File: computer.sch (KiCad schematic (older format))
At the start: 0 parts

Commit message: ram pcb
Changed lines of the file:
@@
 $Descr A4 11693 8268
 encoding utf-8
-Sheet 1 13
+Sheet 1 12
 Title ""
 Date ""
@@
 Wire Bus Line
 	5100 2025 4725 2025
-$Sheet
-S 3575 2750 1100 775
-U 5D35D52D
-F0 "RAM" 50
-F1 "RAM.sch" 50
-F2 "A_BUS[0..15]" I L 3575 2850 50
-F3 "D_BUS[0..15]" B R 4675 3075 50
-F4 "~WE~" I L 3575 3000 50
-F5 "~CE~" I L 3575 3100 50
-F6 "~OE~" I L 3575 3200 50
-F7 "P[0..15]" I L 3575 3450 50
-F8 "~ENABLE_OUTPUT~" I L 3575 3300 50
-$EndSheet
 Wire Bus Line
 	5075 3075 4675 3075
@@
 Wire Bus Line
 	3275 2850 3575 2850
+$Sheet
+S 3575 2775 1100 625
+U 5EEA4AC8
+F0 "RAM" 50
+F1 "memory/memory.sch" 50
+F2 "A[0..15]" I L 3575 2850 50
+F3 "D[0..15]" B R 4675 3075 50
+F4 "~BE~" I L 3575 2975 50
+F5 "~R~-W" I L 3575 3075 50
+$EndSheet
 $EndSCHEMATC

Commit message: program counter
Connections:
- wire segments 8 -> 10
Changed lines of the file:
@@
 	4700 1175 5000 1175
-Wire Wire Line
-	5000 1175 5000 1875
 Wire Wire Line
 	6250 1875 5000 1875
@@
 Wire Bus Line
 	5100 3075 6250 3075
-Wire Bus Line
-	5100 1175 5100 2025
 Connection ~ 5100 2025
 Wire Bus Line
@@
 F5 "~R~-W" I L 3575 3075 50
 $EndSheet
+$Sheet
+S 6250 975  850  550
+U 5EEFDD90
+F0 "program counter" 50
+F1 "program_counter/program_counter.sch" 50
+F2 "BUS[0..15]" B L 6250 1100 50
+F3 "CLK" I L 6250 1300 50
+F4 "~RESET~" I R 7100 1200 50
+F5 "~LOAD~" I R 7100 1300 50
+F6 "COUNT" I R 7100 1400 50
+F7 "~EO~" I R 7100 1100 50
+$EndSheet
+Wire Bus Line
+	6250 1100 5100 1100
+Wire Bus Line
+	5100 1100 5100 2025
+Wire Wire Line
+	6250 1300 5000 1300
+Wire Wire Line
+	5000 1175 5000 1300
+Connection ~ 5000 1300
+Wire Wire Line
+	5000 1300 5000 1875
 $EndSCHEMATC

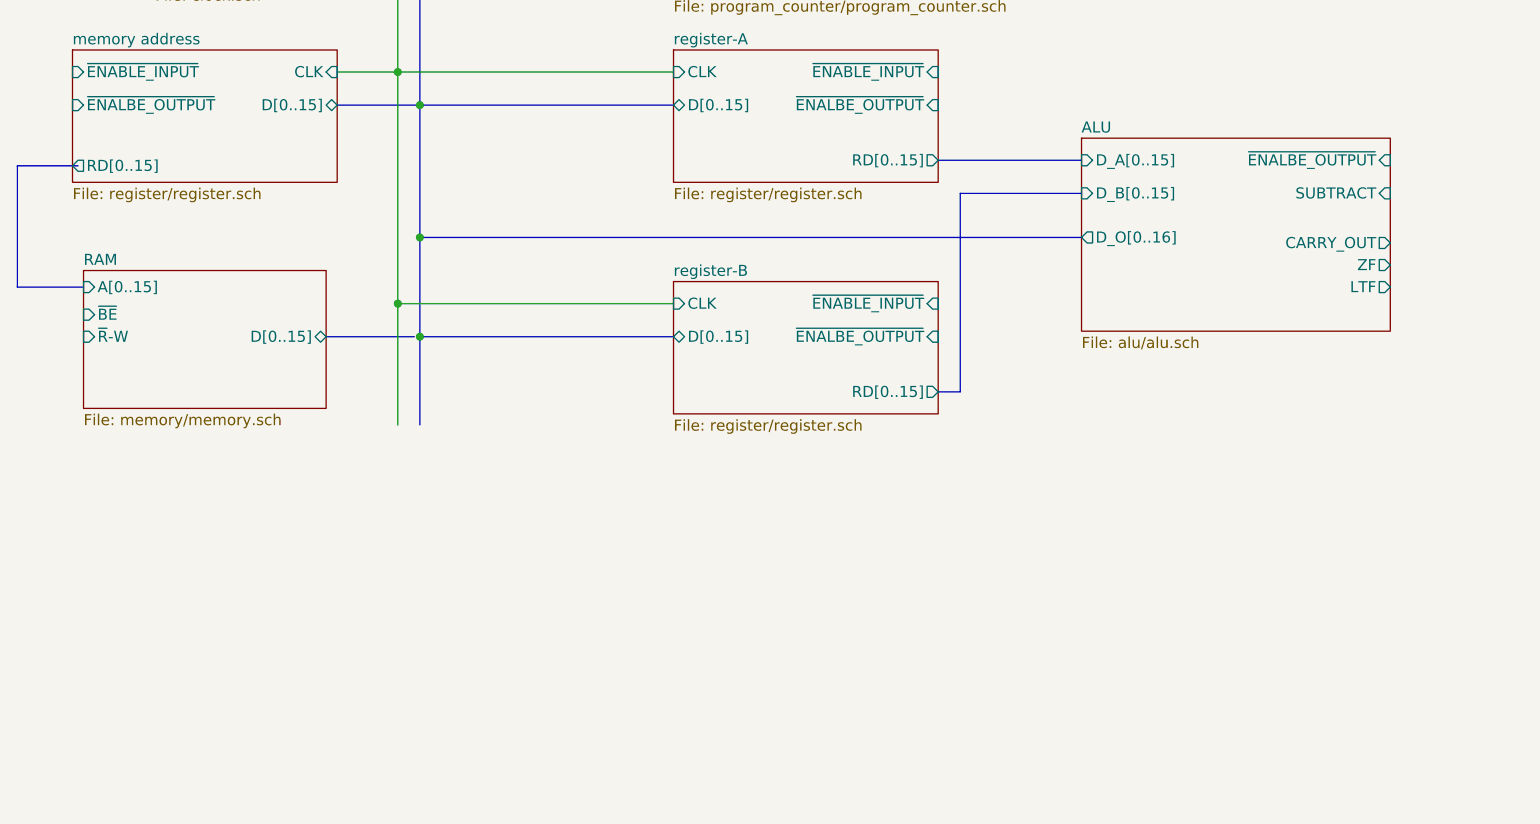
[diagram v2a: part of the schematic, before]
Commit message: add bit operations
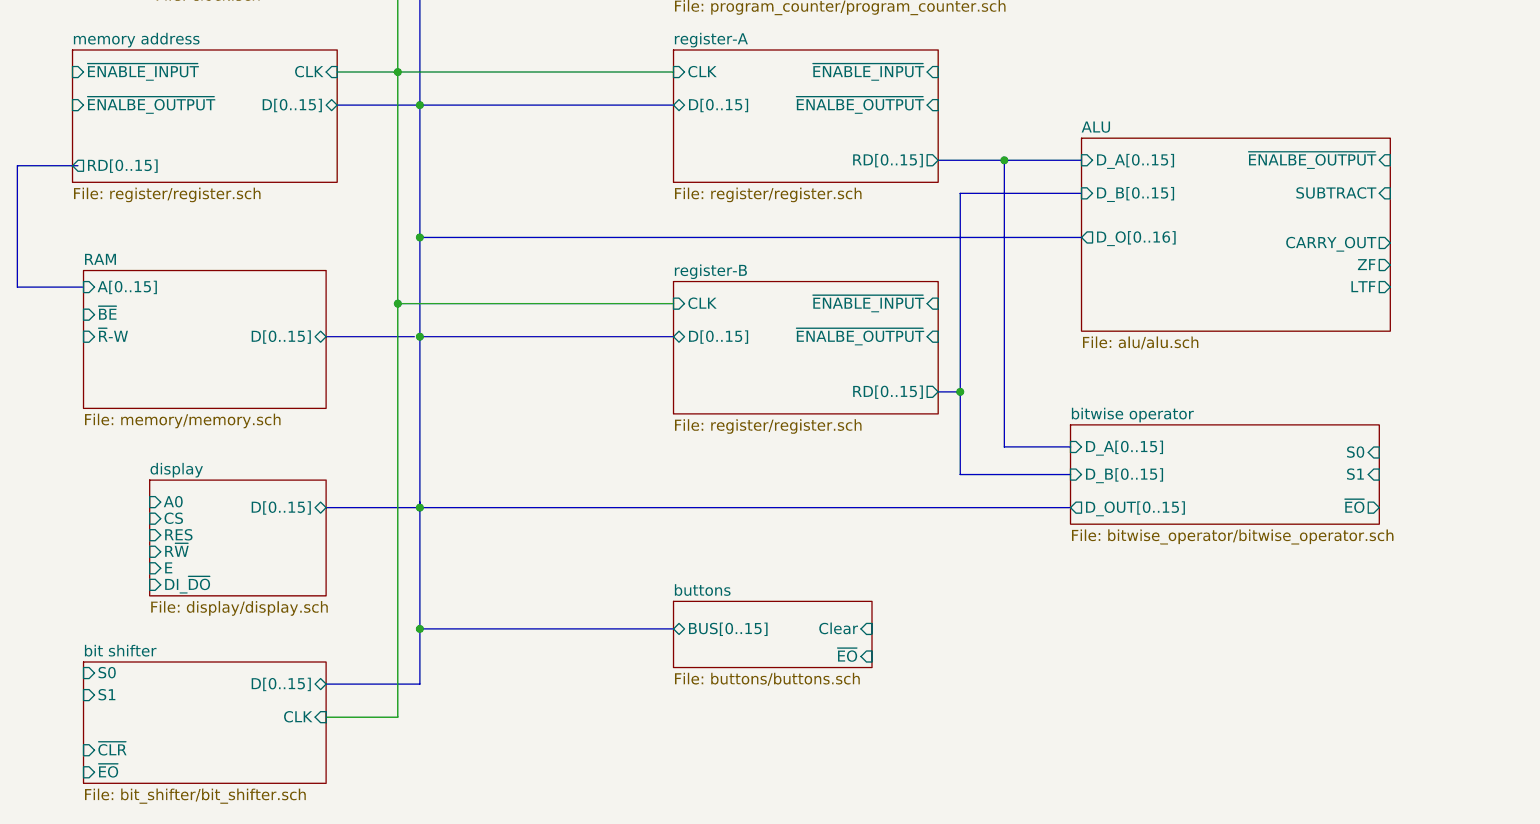
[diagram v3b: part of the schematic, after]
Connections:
- wire segments 10 -> 11
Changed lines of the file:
@@
 $Descr A4 11693 8268
 encoding utf-8
-Sheet 1 12
+Sheet 1 29
 Title ""
 Date ""
@@
 	6250 2925 5000 2925
 Connection ~ 5000 2925
-Wire Wire Line
-	5000 2925 5000 3475
 Wire Bus Line
 	6250 2025 5100 2025
@@
 	5100 2025 5100 2625
 Connection ~ 5100 3075
-Wire Bus Line
-	5100 3075 5100 3475
 $Sheet
 S 8100 2175 1400 875
@@
 $EndSheet
 Wire Bus Line
-	7450 2275 8100 2275
+	7450 2275 7750 2275
 Wire Bus Line
 	7450 3325 7550 3325
-Wire Bus Line
-	7550 3325 7550 2425
 Wire Bus Line
 	7550 2425 8100 2425
@@
 Wire Wire Line
 	5000 1300 5000 1875
+$Sheet
+S 8050 3475 1400 450
+U 5F3A84CD
+F0 "bitwise operator" 50
+F1 "bitwise_operator/bitwise_operator.sch" 50
+F2 "D_A[0..15]" I L 8050 3575 50
+F3 "D_B[0..15]" I L 8050 3700 50
+F4 "S0" I R 9450 3600 50
+F5 "S1" I R 9450 3700 50
+F6 "D_OUT[0..15]" O L 8050 3850 50
+F7 "~EO~" O R 9450 3850 50
+$EndSheet
+Wire Bus Line
+	8050 3700 7550 3700
+Wire Bus Line
+	7550 2425 7550 3325
+Connection ~ 7550 3325
+Wire Bus Line
+	7550 3325 7550 3700
+Wire Bus Line
+	8050 3575 7750 3575
+Wire Bus Line
+	7750 3575 7750 2275
+Connection ~ 7750 2275
+Wire Bus Line
+	7750 2275 8100 2275
+Wire Bus Line
+	8050 3850 5100 3850
+Wire Bus Line
+	5100 3075 5100 3850
+$Sheet
+S 6250 4275 900  300
+U 5F3A94D5
+F0 "buttons" 50
+F1 "buttons/buttons.sch" 50
+F2 "Clear" I R 7150 4400 50
+F3 "~EO~" I R 7150 4525 50
+F4 "BUS[0..15]" B L 6250 4400 50
+$EndSheet
+Wire Bus Line
+	5100 3850 5100 4400
+Wire Bus Line
+	5100 4400 6250 4400
+Connection ~ 5100 3850
+Wire Bus Line
+	5100 3850 5100 3825
+$Sheet
+S 3575 4550 1100 550
+U 5F3AB933
+F0 "bit shifter" 50
+F1 "bit_shifter/bit_shifter.sch" 50
+F2 "D[0..15]" B R 4675 4650 50
+F3 "S0" I L 3575 4600 50
+F4 "S1" I L 3575 4700 50
+F5 "CLK" I R 4675 4800 50
+F6 "~CLR~" I L 3575 4950 50
+F7 "~EO~" I L 3575 5050 50
+$EndSheet
+Wire Bus Line
+	5100 4400 5100 4650
+Wire Bus Line
+	5100 4650 4675 4650
+Connection ~ 5100 4400
+Wire Wire Line
+	5000 4800 4675 4800
+Wire Wire Line
+	5000 2925 5000 4800
+Wire Bus Line
+	4675 3850 5100 3850
+$Sheet
+S 3875 3725 800  525
+U 5F3B052B
+F0 "display" 50
+F1 "display/display.sch" 50
+F2 "D[0..15]" B R 4675 3850 50
+F3 "A0" I L 3875 3825 50
+F4 "CS" I L 3875 3900 50
+F5 "RES" I L 3875 3975 50
+F6 "R~W~" I L 3875 4050 50
+F7 "E" I L 3875 4125 50
+F8 "DI_~DO~" I L 3875 4200 50
+$EndSheet
 $EndSCHEMATC

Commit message: memory programmer and cu
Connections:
- net labels added: D_10, D_11, D_8, D_9, GND
- wire segments 11 -> 19
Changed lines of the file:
@@
 F5 "S1" I R 9450 3700 50
 F6 "D_OUT[0..15]" O L 8050 3850 50
-F7 "~EO~" O R 9450 3850 50
+F7 "~EO~" I R 9450 3850 50
 $EndSheet
 Wire Bus Line
@@
 F8 "DI_~DO~" I L 3875 4200 50
 $EndSheet
+$Sheet
+S 6275 5550 975  500
+U 5F3E0C36
+F0 "control unit" 50
+F1 "control_unit/control_unit.sch" 50
+F2 "CLK" I L 6275 5600 50
+F3 "FLG_[0..3]" I L 6275 5700 50
+F4 "I_[0..15]" I L 6275 5800 50
+F5 "IL_[0..3]" O R 7250 5625 50
+F6 "IL_FL_[0..3]" I R 7250 5700 50
+F7 "D_[8..11]" I R 7250 5800 50
+$EndSheet
+Wire Bus Line
+	7250 5625 7375 5625
+Wire Bus Line
+	7375 5625 7375 5700
+Wire Bus Line
+	7375 5700 7250 5700
+Entry Wire Line
+	7550 5800 7650 5900
+Wire Wire Line
+	7650 6150 7725 6150
+Text Label 7650 6100 1    50   ~ 0
+D_8
+Entry Wire Line
+	7625 5800 7725 5900
+Text Label 7725 6100 1    50   ~ 0
+D_9
+Entry Wire Line
+	7700 5800 7800 5900
+Text Label 7800 6100 1    50   ~ 0
+D_10
+Entry Wire Line
+	7775 5800 7875 5900
+Text Label 7875 6100 1    50   ~ 0
+D_11
+Connection ~ 7725 6150
+Wire Wire Line
+	7725 6150 7800 6150
+Connection ~ 7800 6150
+Wire Wire Line
+	7800 6150 7875 6150
+Connection ~ 7875 6150
+Wire Wire Line
+	7875 6150 7950 6150
+$Comp
+L power:GND #PWR?
+U 1 1 5F3E45F1
+P 7950 6150
+F 0 "#PWR?" H 7950 5900 50  0001 C CNN
+F 1 "GND" V 7955 6022 50  0000 R CNN
+F 2 "" H 7950 6150 50  0001 C CNN
+F 3 "" H 7950 6150 50  0001 C CNN
+	1    7950 6150
+	0    -1   -1   0
+$EndComp
+Wire Wire Line
+	7875 5900 7875 6150
+Wire Wire Line
+	7800 5900 7800 6150
+Wire Wire Line
+	7725 5900 7725 6150
+Wire Wire Line
+	7650 5900 7650 6150
+Wire Bus Line
+	7250 5800 7775 5800
 $EndSCHEMATC

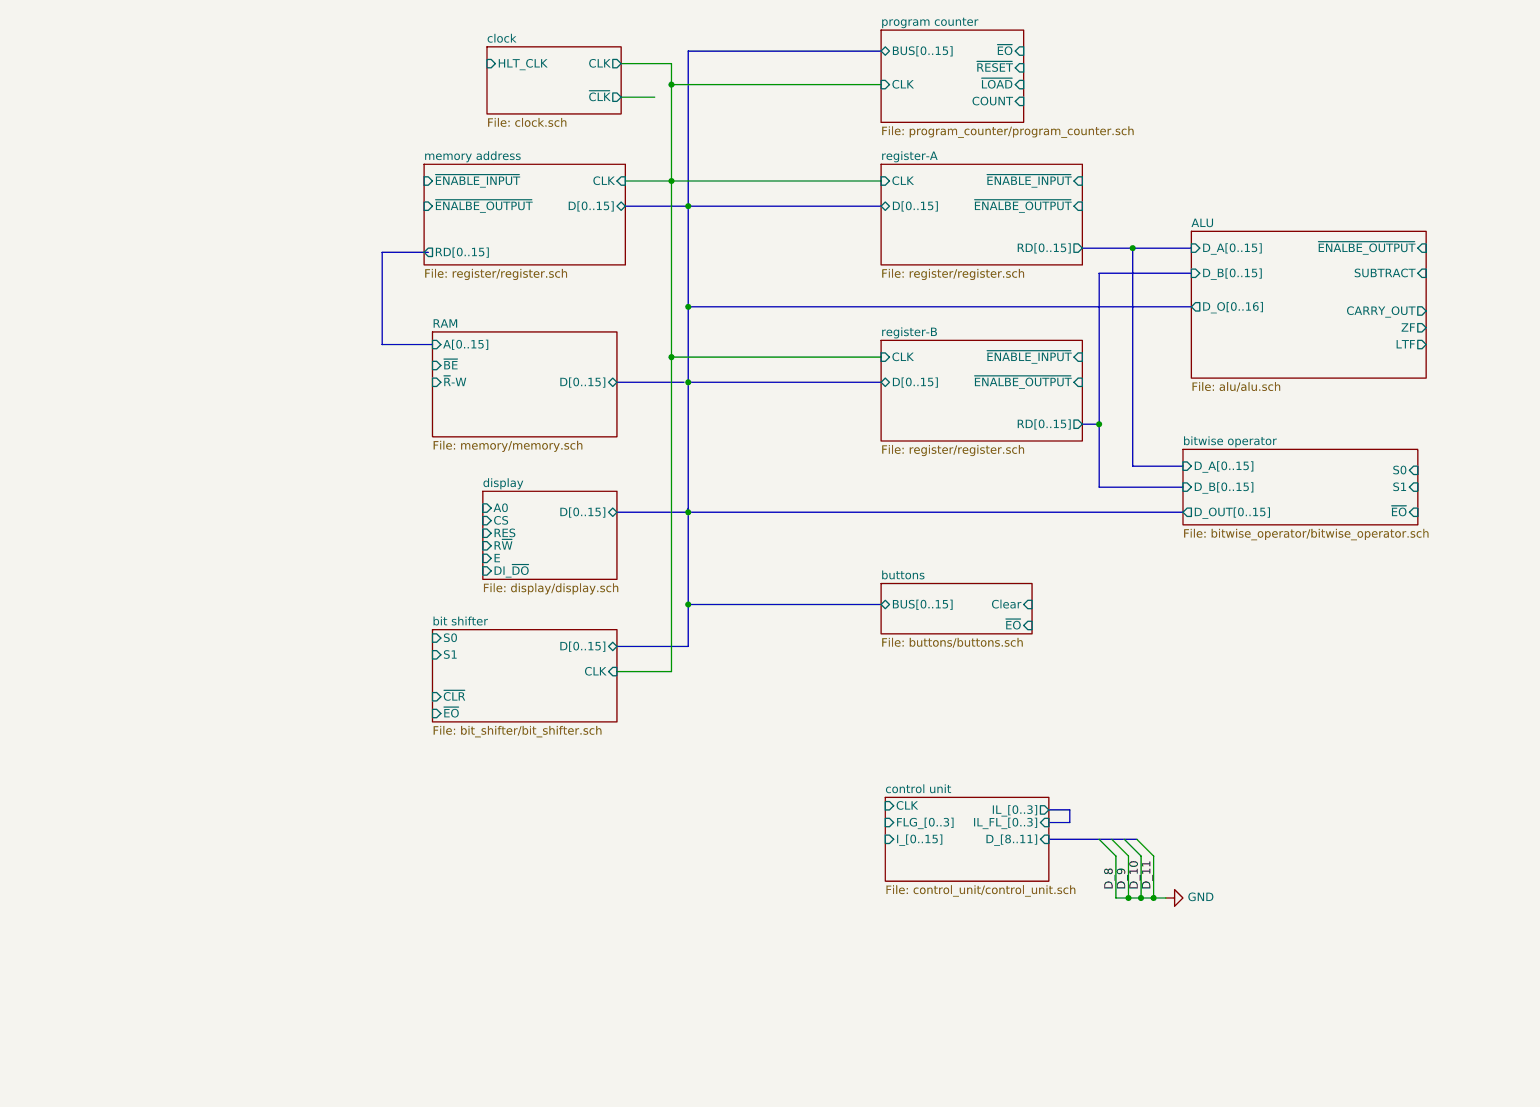
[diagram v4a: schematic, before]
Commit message: connect cu and start creating material csv
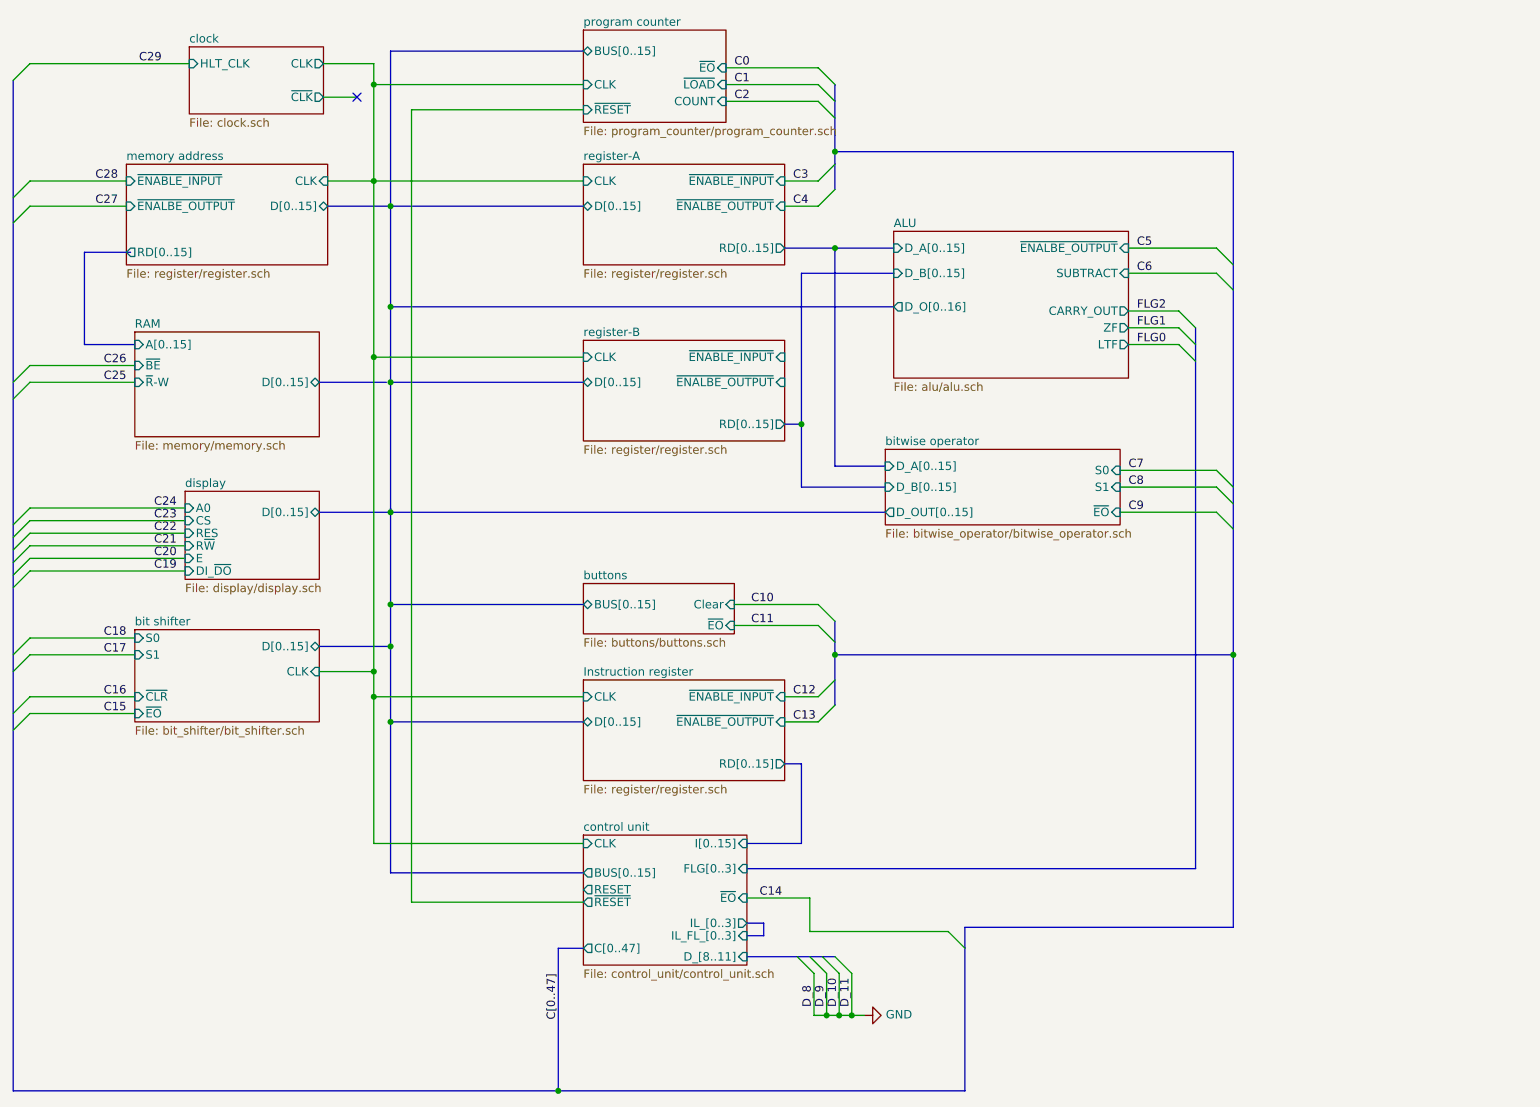
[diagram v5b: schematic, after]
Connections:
- net labels added: C0, C1, C10, C11, C12, C13, C14, C15, C16, C17, C18, C19, C2, C20, C21, C22, C23, C24, C25, C26, C27, C28, C29, C3, C4, C5, C6, C7, C8, C9, C[0..47], FLG0, FLG1, FLG2
- wire segments 19 -> 61
- no-connect marks 0 -> 1
